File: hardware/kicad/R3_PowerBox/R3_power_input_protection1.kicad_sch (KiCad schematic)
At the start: 13 parts, among them J1 SERVICE / BENCH INPUT 6-12V, Q1 DMP3010LSS-13

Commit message: Finalize R3 PowerBox pre-placement corrections
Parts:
- D1: value SMBJ10A -> SMBJ13A / 13V VRWM

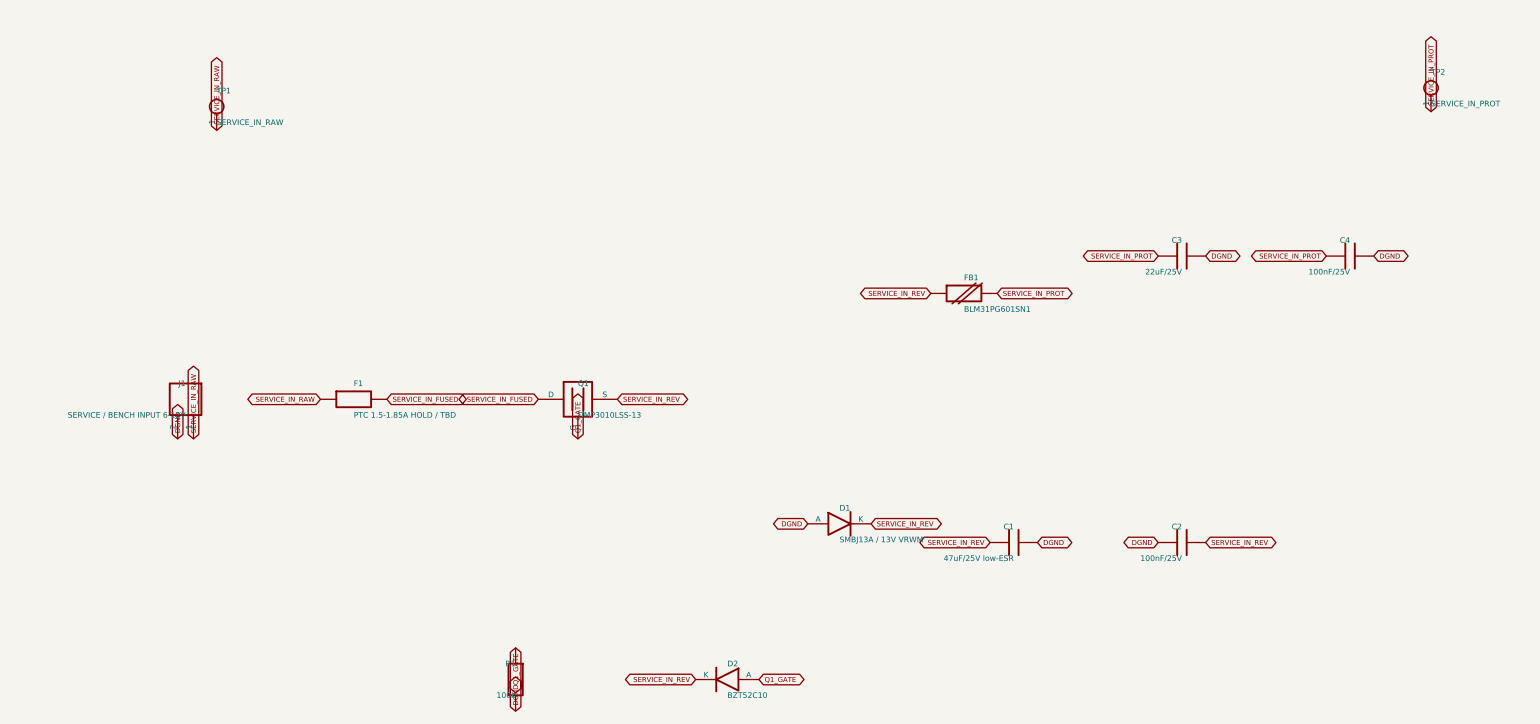
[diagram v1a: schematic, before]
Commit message: Finalize R3 PowerBox pre-routing placement
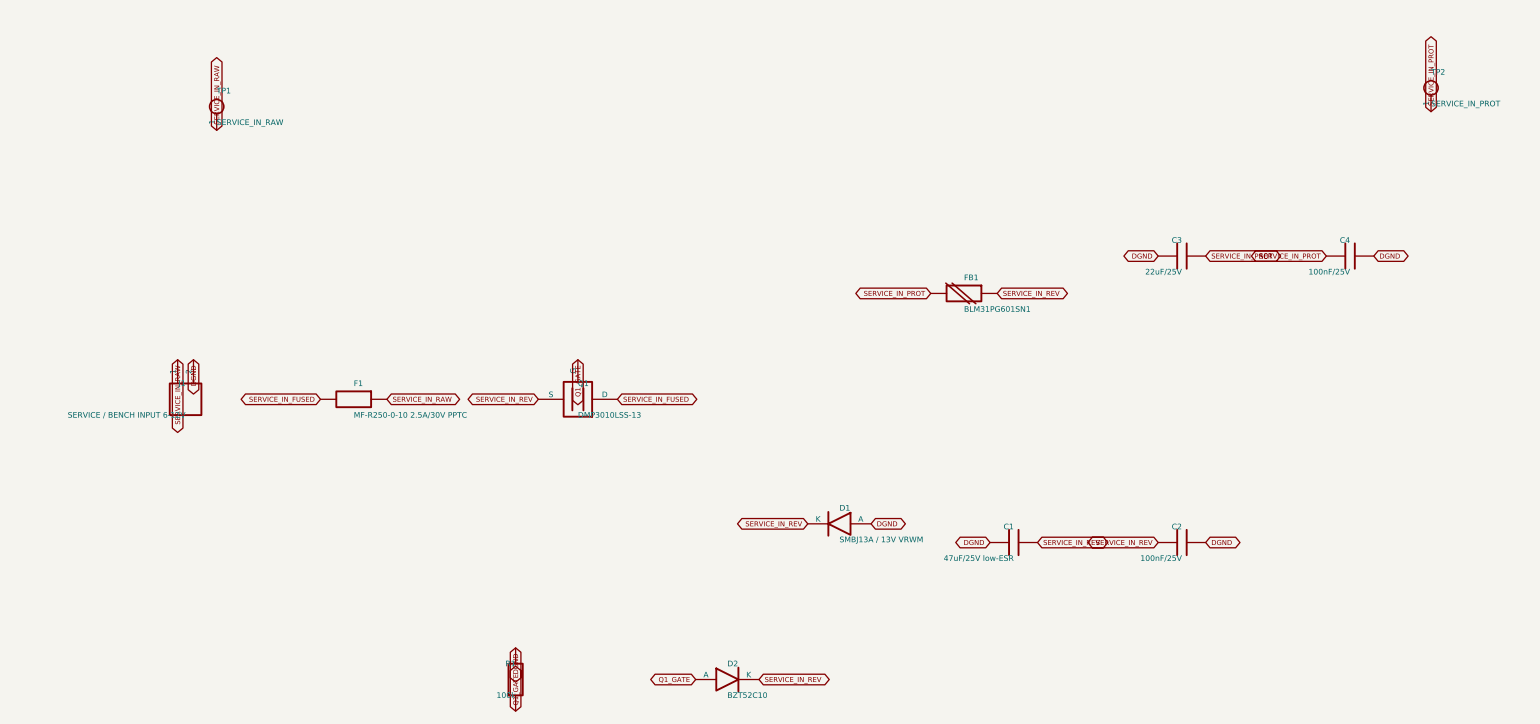
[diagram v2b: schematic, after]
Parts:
- F1: value PTC 1.5-1.85A HOLD / TBD -> MF-R250-0-10 2.5A/30V PPTC; footprint R3_Power:Fuse_PTC_MF-R160_R185_Class -> R3_Power:Fuse_PTC_MF-R250
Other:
- moved on the sheet: C1, C2, C3, D1, F1, FB1, J1, Q1, R1

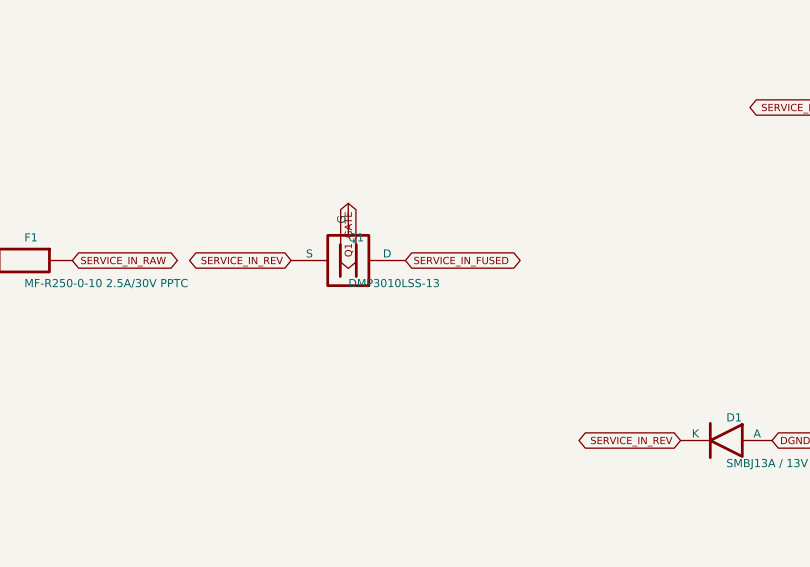
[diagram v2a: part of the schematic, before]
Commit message: Finalize R3 PowerBox user power controls
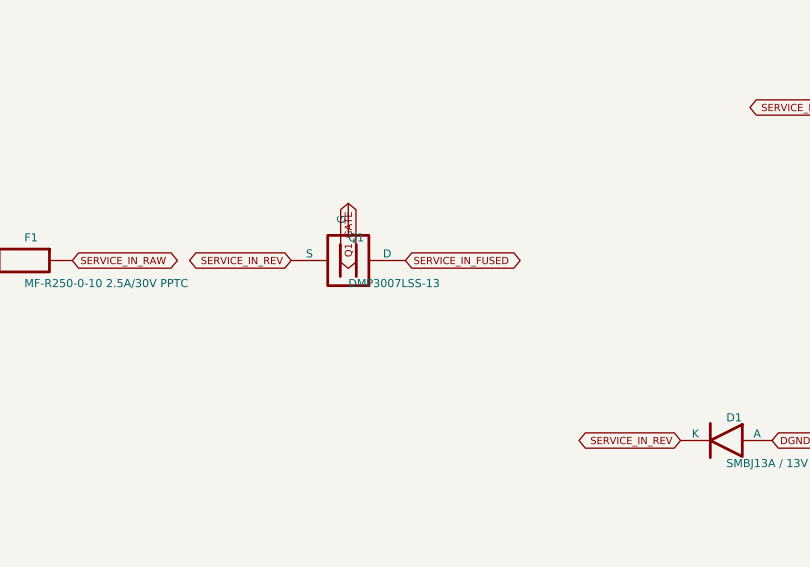
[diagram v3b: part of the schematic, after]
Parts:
- Q1: value DMP3010LSS-13 -> DMP3007LSS-13; footprint Package_SO:SO-8_3.9x4.9mm_P1.27mm -> R3_Power:DMP3007LSS_SO8_LOGICAL
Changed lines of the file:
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@@
     (instances
       (project "SKiDL-Generated"
-        (path "/a017fe2a-e7ec-4366-869f-7432dcfdc1ce/5da63eac-35bb-5462-8a73-576e5b60132e"
+        (path "/ed43c75e-de56-4b8e-bb37-9a897af3b629/5da63eac-35bb-5462-8a73-576e5b60132e"
           (reference "J1")
           (unit 1)))))
@@
     (instances
       (project "SKiDL-Generated"
-        (path "/a017fe2a-e7ec-4366-869f-7432dcfdc1ce/5da63eac-35bb-5462-8a73-576e5b60132e"
+        (path "/ed43c75e-de56-4b8e-bb37-9a897af3b629/5da63eac-35bb-5462-8a73-576e5b60132e"
           (reference "F1")
           (unit 1)))))
@@
           (size 0.9 0.9))
         (justify left)))
-    (property "Value" "DMP3010LSS-13"
+    (property "Value" "DMP3007LSS-13"
       (at 108 107.54 180)
       (effects
@@
           (size 0.9 0.9))
         (justify left)))
-    (property "Footprint" "Package_SO:SO-8_3.9x4.9mm_P1.27mm"
+    (property "Footprint" "R3_Power:DMP3007LSS_SO8_LOGICAL"
       (at 108 105 180)
       (effects
@@
           (size 0.9 0.9))
         (hide yes)))
-    (property "Datasheet" "~"
+    (property "Datasheet" "https://www.diodes.com/part/view/DMP3007LSS"
       (at 108 105 180)
       (effects
@@
     (instances
       (project "SKiDL-Generated"
-        (path "/a017fe2a-e7ec-4366-869f-7432dcfdc1ce/5da63eac-35bb-5462-8a73-576e5b60132e"
+        (path "/ed43c75e-de56-4b8e-bb37-9a897af3b629/5da63eac-35bb-5462-8a73-576e5b60132e"
           (reference "Q1")
           (unit 1)))))
@@
     (instances
       (project "SKiDL-Generated"
-        (path "/a017fe2a-e7ec-4366-869f-7432dcfdc1ce/5da63eac-35bb-5462-8a73-576e5b60132e"
+        (path "/ed43c75e-de56-4b8e-bb37-9a897af3b629/5da63eac-35bb-5462-8a73-576e5b60132e"
           (reference "R1")
           (unit 1)))))
@@
     (instances
       (project "SKiDL-Generated"
-        (path "/a017fe2a-e7ec-4366-869f-7432dcfdc1ce/5da63eac-35bb-5462-8a73-576e5b60132e"
+        (path "/ed43c75e-de56-4b8e-bb37-9a897af3b629/5da63eac-35bb-5462-8a73-576e5b60132e"
           (reference "D2")
           (unit 1)))))
@@
     (instances
       (project "SKiDL-Generated"
-        (path "/a017fe2a-e7ec-4366-869f-7432dcfdc1ce/5da63eac-35bb-5462-8a73-576e5b60132e"
+        (path "/ed43c75e-de56-4b8e-bb37-9a897af3b629/5da63eac-35bb-5462-8a73-576e5b60132e"
           (reference "D1")
           (unit 1)))))
@@
     (instances
       (project "SKiDL-Generated"
-        (path "/a017fe2a-e7ec-4366-869f-7432dcfdc1ce/5da63eac-35bb-5462-8a73-576e5b60132e"
+        (path "/ed43c75e-de56-4b8e-bb37-9a897af3b629/5da63eac-35bb-5462-8a73-576e5b60132e"
           (reference "C1")
           (unit 1)))))
@@
     (instances
       (project "SKiDL-Generated"
-        (path "/a017fe2a-e7ec-4366-869f-7432dcfdc1ce/5da63eac-35bb-5462-8a73-576e5b60132e"
+        (path "/ed43c75e-de56-4b8e-bb37-9a897af3b629/5da63eac-35bb-5462-8a73-576e5b60132e"
           (reference "C2")
           (unit 1)))))
@@
     (instances
       (project "SKiDL-Generated"
-        (path "/a017fe2a-e7ec-4366-869f-7432dcfdc1ce/5da63eac-35bb-5462-8a73-576e5b60132e"
+        (path "/ed43c75e-de56-4b8e-bb37-9a897af3b629/5da63eac-35bb-5462-8a73-576e5b60132e"
           (reference "FB1")
           (unit 1)))))
@@
     (instances
       (project "SKiDL-Generated"
-        (path "/a017fe2a-e7ec-4366-869f-7432dcfdc1ce/5da63eac-35bb-5462-8a73-576e5b60132e"
+        (path "/ed43c75e-de56-4b8e-bb37-9a897af3b629/5da63eac-35bb-5462-8a73-576e5b60132e"
           (reference "C3")
           (unit 1)))))
@@
     (instances
       (project "SKiDL-Generated"
-        (path "/a017fe2a-e7ec-4366-869f-7432dcfdc1ce/5da63eac-35bb-5462-8a73-576e5b60132e"
+        (path "/ed43c75e-de56-4b8e-bb37-9a897af3b629/5da63eac-35bb-5462-8a73-576e5b60132e"
           (reference "C4")
           (unit 1)))))
@@
     (instances
       (project "SKiDL-Generated"
-        (path "/a017fe2a-e7ec-4366-869f-7432dcfdc1ce/5da63eac-35bb-5462-8a73-576e5b60132e"
+        (path "/ed43c75e-de56-4b8e-bb37-9a897af3b629/5da63eac-35bb-5462-8a73-576e5b60132e"
           (reference "TP1")
           (unit 1)))))
@@
     (instances
       (project "SKiDL-Generated"
-        (path "/a017fe2a-e7ec-4366-869f-7432dcfdc1ce/5da63eac-35bb-5462-8a73-576e5b60132e"
+        (path "/ed43c75e-de56-4b8e-bb37-9a897af3b629/5da63eac-35bb-5462-8a73-576e5b60132e"
           (reference "TP2")
           (unit 1)))))

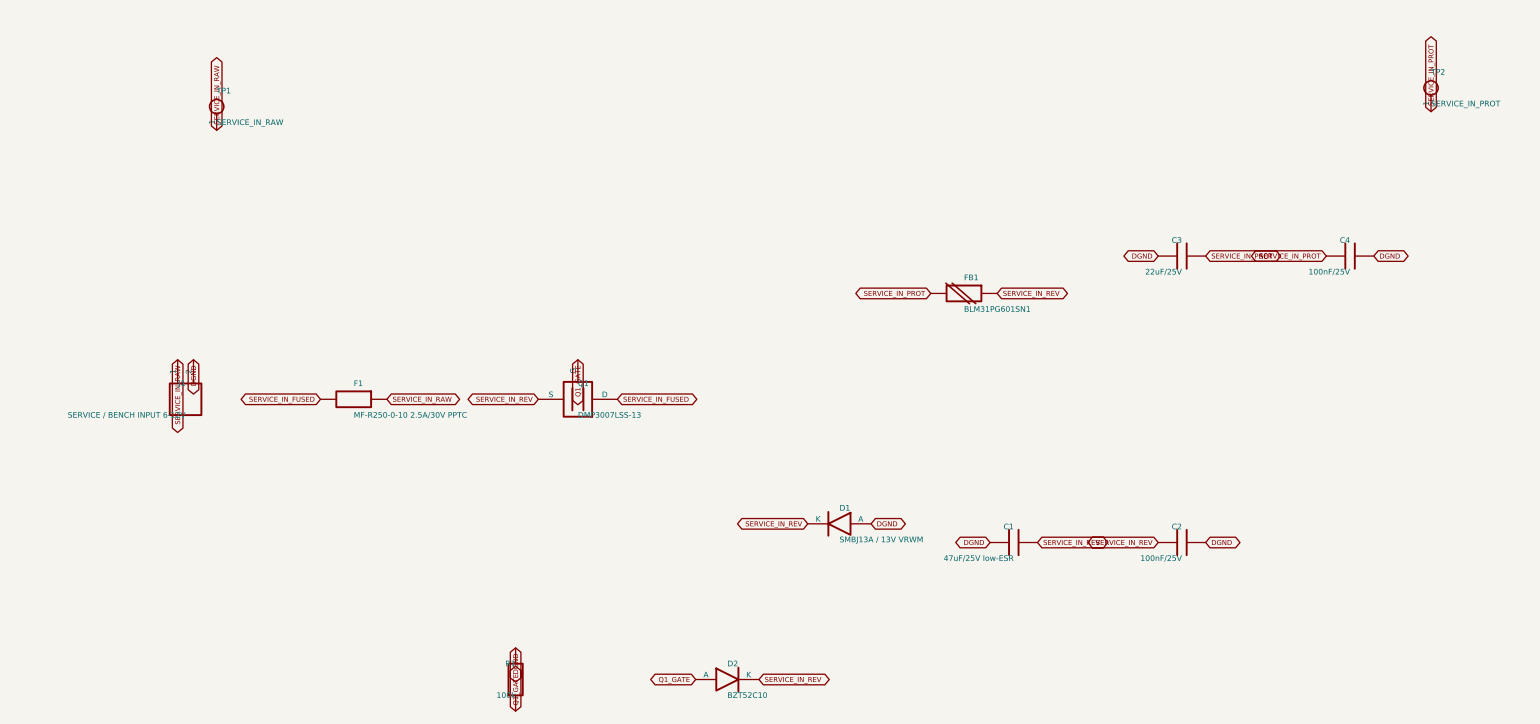
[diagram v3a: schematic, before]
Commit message: Finalize R3 PowerBox mechanical interconnect
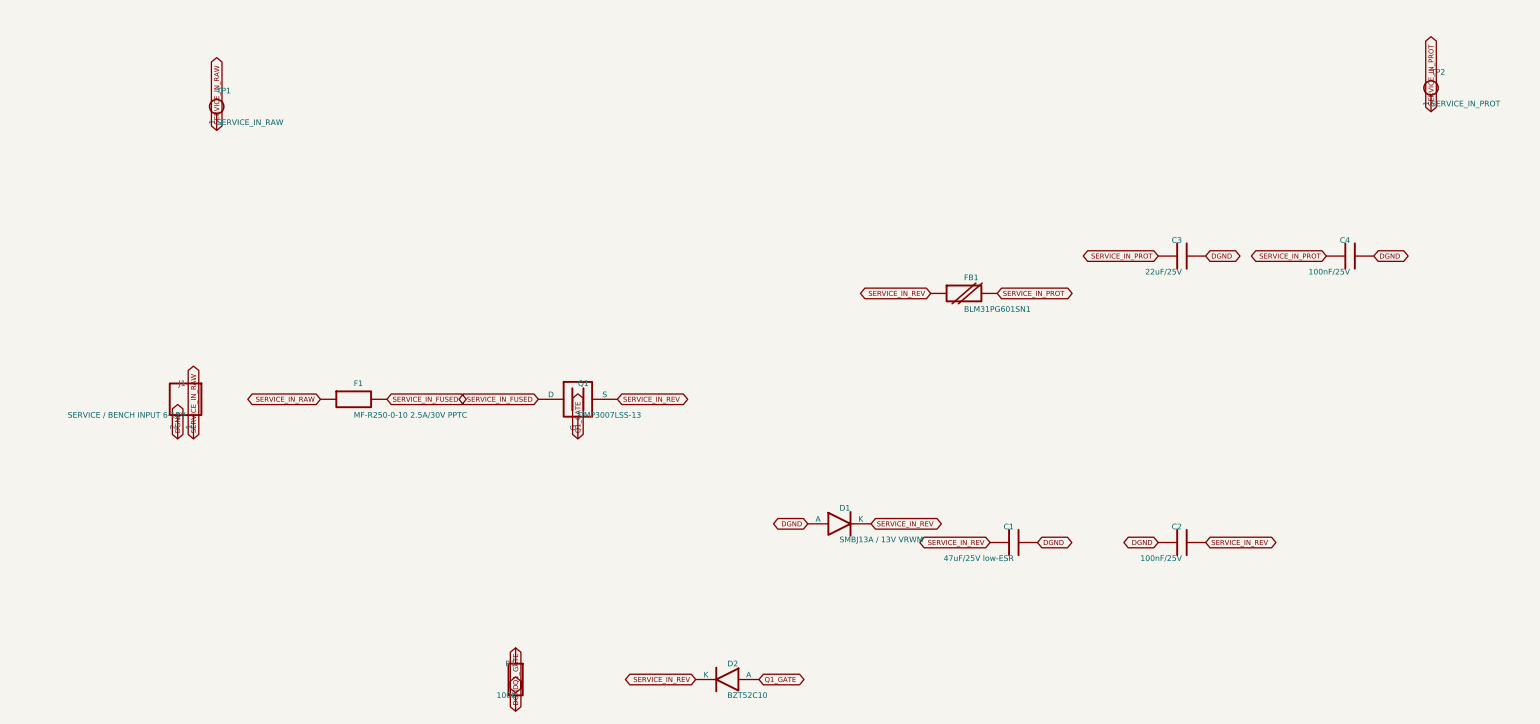
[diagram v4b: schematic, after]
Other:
- moved on the sheet: C1, C2, C3, D1, D2, F1, FB1, J1, Q1, R1

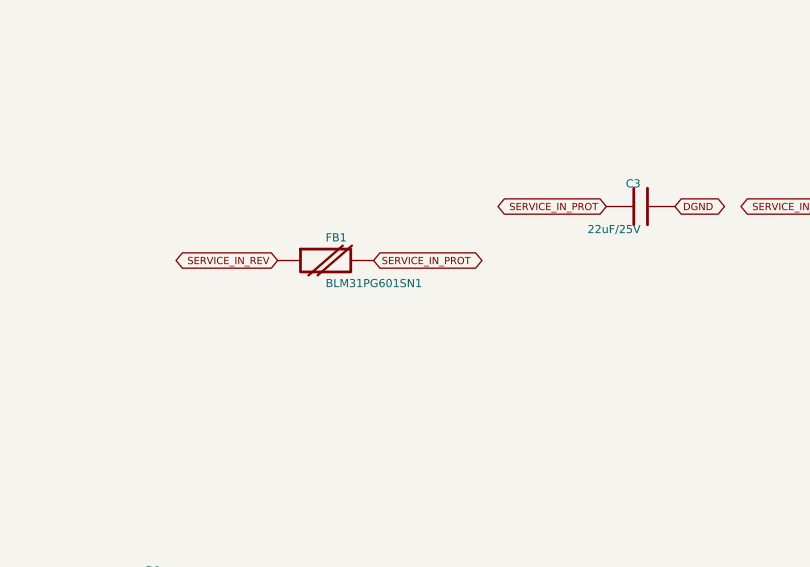
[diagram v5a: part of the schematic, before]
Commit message: Rev.A review fixes: initial schematic and component corrections
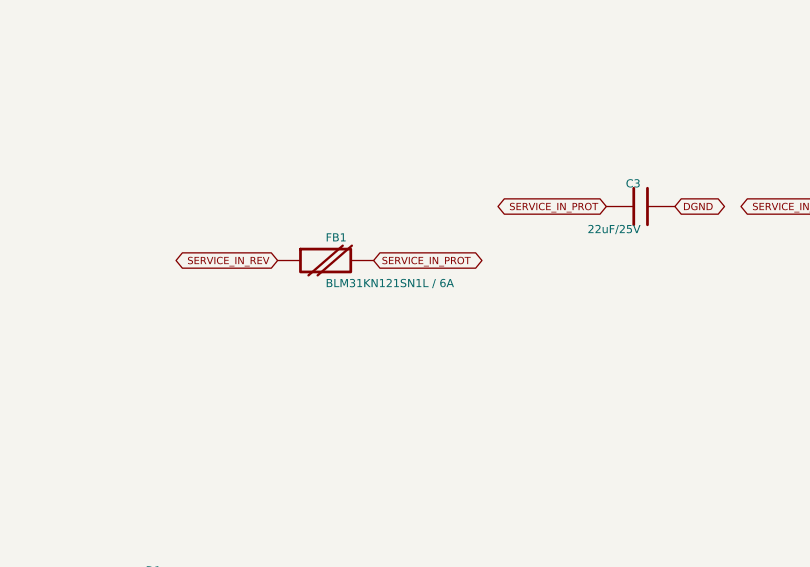
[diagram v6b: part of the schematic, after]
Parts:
- FB1: value BLM31PG601SN1 -> BLM31KN121SN1L / 6A
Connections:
- net DGND: now also D1.2 (A); no longer D1.1 (A)
- net Q1_GATE: now also D2.2 (A); no longer D2.1 (A)
- net SERVICE_IN_REV: now also D1.1 (K), D2.1 (K); no longer D1.2 (K), D2.2 (K)
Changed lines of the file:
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@@
   (title_block
     (title "R3 PowerBox — power tree")
-    (date "2026-09-28")
+    (date "2026-10-03")
     (company "")
     (comment 1 "Generated with SKiDL")
@@
     (instances
       (project "SKiDL-Generated"
-        (path "/c950aac3-a7f8-40a1-8854-63ca2e6194cc/5da63eac-35bb-5462-8a73-576e5b60132e"
+        (path "/7d40ec76-f97b-4a90-b5ea-ddf1628062b5/5da63eac-35bb-5462-8a73-576e5b60132e"
           (reference "J1")
           (unit 1)))))
@@
     (instances
       (project "SKiDL-Generated"
-        (path "/c950aac3-a7f8-40a1-8854-63ca2e6194cc/5da63eac-35bb-5462-8a73-576e5b60132e"
+        (path "/7d40ec76-f97b-4a90-b5ea-ddf1628062b5/5da63eac-35bb-5462-8a73-576e5b60132e"
           (reference "F1")
           (unit 1)))))
@@
     (instances
       (project "SKiDL-Generated"
-        (path "/c950aac3-a7f8-40a1-8854-63ca2e6194cc/5da63eac-35bb-5462-8a73-576e5b60132e"
+        (path "/7d40ec76-f97b-4a90-b5ea-ddf1628062b5/5da63eac-35bb-5462-8a73-576e5b60132e"
           (reference "Q1")
           (unit 1)))))
@@
     (instances
       (project "SKiDL-Generated"
-        (path "/c950aac3-a7f8-40a1-8854-63ca2e6194cc/5da63eac-35bb-5462-8a73-576e5b60132e"
+        (path "/7d40ec76-f97b-4a90-b5ea-ddf1628062b5/5da63eac-35bb-5462-8a73-576e5b60132e"
           (reference "R1")
           (unit 1)))))
@@
           (size 0.9 0.9))
         (hide yes)))
-    (pin "1"
-)
-    (pin "2"
-)
-    (instances
-      (project "SKiDL-Generated"
-        (path "/c950aac3-a7f8-40a1-8854-63ca2e6194cc/5da63eac-35bb-5462-8a73-576e5b60132e"
+    (pin "2"
+)
+    (pin "1"
+)
+    (instances
+      (project "SKiDL-Generated"
+        (path "/7d40ec76-f97b-4a90-b5ea-ddf1628062b5/5da63eac-35bb-5462-8a73-576e5b60132e"
           (reference "D2")
           (unit 1)))))
@@
           (size 0.9 0.9))
         (hide yes)))
-    (pin "1"
-)
-    (pin "2"
-)
-    (instances
-      (project "SKiDL-Generated"
-        (path "/c950aac3-a7f8-40a1-8854-63ca2e6194cc/5da63eac-35bb-5462-8a73-576e5b60132e"
+    (pin "2"
+)
+    (pin "1"
+)
+    (instances
+      (project "SKiDL-Generated"
+        (path "/7d40ec76-f97b-4a90-b5ea-ddf1628062b5/5da63eac-35bb-5462-8a73-576e5b60132e"
           (reference "D1")
           (unit 1)))))
@@
     (instances
       (project "SKiDL-Generated"
-        (path "/c950aac3-a7f8-40a1-8854-63ca2e6194cc/5da63eac-35bb-5462-8a73-576e5b60132e"
+        (path "/7d40ec76-f97b-4a90-b5ea-ddf1628062b5/5da63eac-35bb-5462-8a73-576e5b60132e"
           (reference "C1")
           (unit 1)))))
@@
     (instances
       (project "SKiDL-Generated"
-        (path "/c950aac3-a7f8-40a1-8854-63ca2e6194cc/5da63eac-35bb-5462-8a73-576e5b60132e"
+        (path "/7d40ec76-f97b-4a90-b5ea-ddf1628062b5/5da63eac-35bb-5462-8a73-576e5b60132e"
           (reference "C2")
           (unit 1)))))
@@
           (size 0.9 0.9))
         (justify left)))
-    (property "Value" "BLM31PG601SN1"
+    (property "Value" "BLM31KN121SN1L / 6A"
       (at 170 90.54 0)
       (effects
@@
     (instances
       (project "SKiDL-Generated"
-        (path "/c950aac3-a7f8-40a1-8854-63ca2e6194cc/5da63eac-35bb-5462-8a73-576e5b60132e"
+        (path "/7d40ec76-f97b-4a90-b5ea-ddf1628062b5/5da63eac-35bb-5462-8a73-576e5b60132e"
           (reference "FB1")
           (unit 1)))))
@@
     (instances
       (project "SKiDL-Generated"
-        (path "/c950aac3-a7f8-40a1-8854-63ca2e6194cc/5da63eac-35bb-5462-8a73-576e5b60132e"
+        (path "/7d40ec76-f97b-4a90-b5ea-ddf1628062b5/5da63eac-35bb-5462-8a73-576e5b60132e"
           (reference "C3")
           (unit 1)))))
@@
     (instances
       (project "SKiDL-Generated"
-        (path "/c950aac3-a7f8-40a1-8854-63ca2e6194cc/5da63eac-35bb-5462-8a73-576e5b60132e"
+        (path "/7d40ec76-f97b-4a90-b5ea-ddf1628062b5/5da63eac-35bb-5462-8a73-576e5b60132e"
           (reference "C4")
           (unit 1)))))
@@
     (instances
       (project "SKiDL-Generated"
-        (path "/c950aac3-a7f8-40a1-8854-63ca2e6194cc/5da63eac-35bb-5462-8a73-576e5b60132e"
+        (path "/7d40ec76-f97b-4a90-b5ea-ddf1628062b5/5da63eac-35bb-5462-8a73-576e5b60132e"
           (reference "TP1")
           (unit 1)))))
@@
     (instances
       (project "SKiDL-Generated"
-        (path "/c950aac3-a7f8-40a1-8854-63ca2e6194cc/5da63eac-35bb-5462-8a73-576e5b60132e"
+        (path "/7d40ec76-f97b-4a90-b5ea-ddf1628062b5/5da63eac-35bb-5462-8a73-576e5b60132e"
           (reference "TP2")
           (unit 1)))))
